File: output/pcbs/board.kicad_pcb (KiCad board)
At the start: 2 copper layers, 122.3 x 101.1 mm, 39 parts

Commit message: wip
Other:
- net class Power added: clearance 0.2, trace_width 0.5, via_dia 0.8, via_drill 0.4
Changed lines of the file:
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@@
 (net 39 "P8")
 (net 40 "P9")
-  (net_class Default "This is the default net class."
+  (net_class Default "This is the default net class"
     (clearance 0.2)
     (trace_width 0.25)
@@
 (add_net "home_thumb")
 (add_net "far_thumb")
-(add_net "RAW")
-(add_net "GND")
 (add_net "RST")
-(add_net "VCC")
 (add_net "P14")
 (add_net "P16")
@@
 (add_net "P9")
   )
+  (net_class Power "This is the power net class"
+    (clearance 0.2)
+    (trace_width 0.5)
+    (via_dia 0.8)
+    (via_drill 0.4)
+    (uvia_dia 0.3)
+    (uvia_drill 0.1)
+    (add_net "RAW")
+(add_net "GND")
+(add_net "VCC")
+  )
       (module PG1350 (layer F.Cu)

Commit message: Add output files
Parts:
- moved REF** 2.00 mm to (122.0, -2.20)
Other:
- outline, holes or cut-outs redrawn
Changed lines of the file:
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@@
       )
       (module TRRS-PJ-320A-dual (layer F.Cu)
-      (at 120 -2.1999999999999993 270)
+      (at 122 -2.1999999999999993 270)
       (fp_text reference REF** (at 0 14.2) (layer Dwgs.User) (effects (font (size 1 1) (thickness 0.15))))
       (fp_text value TRRS-PJ-320A-dual (at 0 -5.6) (layer F.Fab) (effects (font (size 1 1) (thickness 0.15))))
@@
 (gr_arc (start 120 -49.85000000000001) (end 122 -49.85000000000001) (angle -90) (layer Edge.Cuts) (width 0.15))
 (gr_line (start 120 -51.85000000000001) (end 99.9943671 -51.85) (angle 90) (layer Edge.Cuts) (width 0.15))
-(gr_circle (center 27 -28.9) (end 28.9 -28.9) (layer Edge.Cuts) (width 0.15))
-(gr_circle (center 27 0) (end 28.9 0) (layer Edge.Cuts) (width 0.15))
-(gr_circle (center 81 -44.2) (end 82.9 -44.2) (layer Edge.Cuts) (width 0.15))
-(gr_circle (center 72 6.119999999999999) (end 73.9 6.119999999999999) (layer Edge.Cuts) (width 0.15))
-(gr_circle (center 110.3491337 22.311939099999996) (end 112.2491337 22.311939099999996) (layer Edge.Cuts) (width 0.15))
+(gr_circle (center 27 -28.9) (end 29.05 -28.9) (layer Edge.Cuts) (width 0.15))
+(gr_circle (center 27 0) (end 29.05 0) (layer Edge.Cuts) (width 0.15))
+(gr_circle (center 81 -44.2) (end 83.05 -44.2) (layer Edge.Cuts) (width 0.15))
+(gr_circle (center 72 6.119999999999999) (end 74.05 6.119999999999999) (layer Edge.Cuts) (width 0.15))
+(gr_circle (center 110.3491337 22.311939099999996) (end 112.3991337 22.311939099999996) (layer Edge.Cuts) (width 0.15))
 )

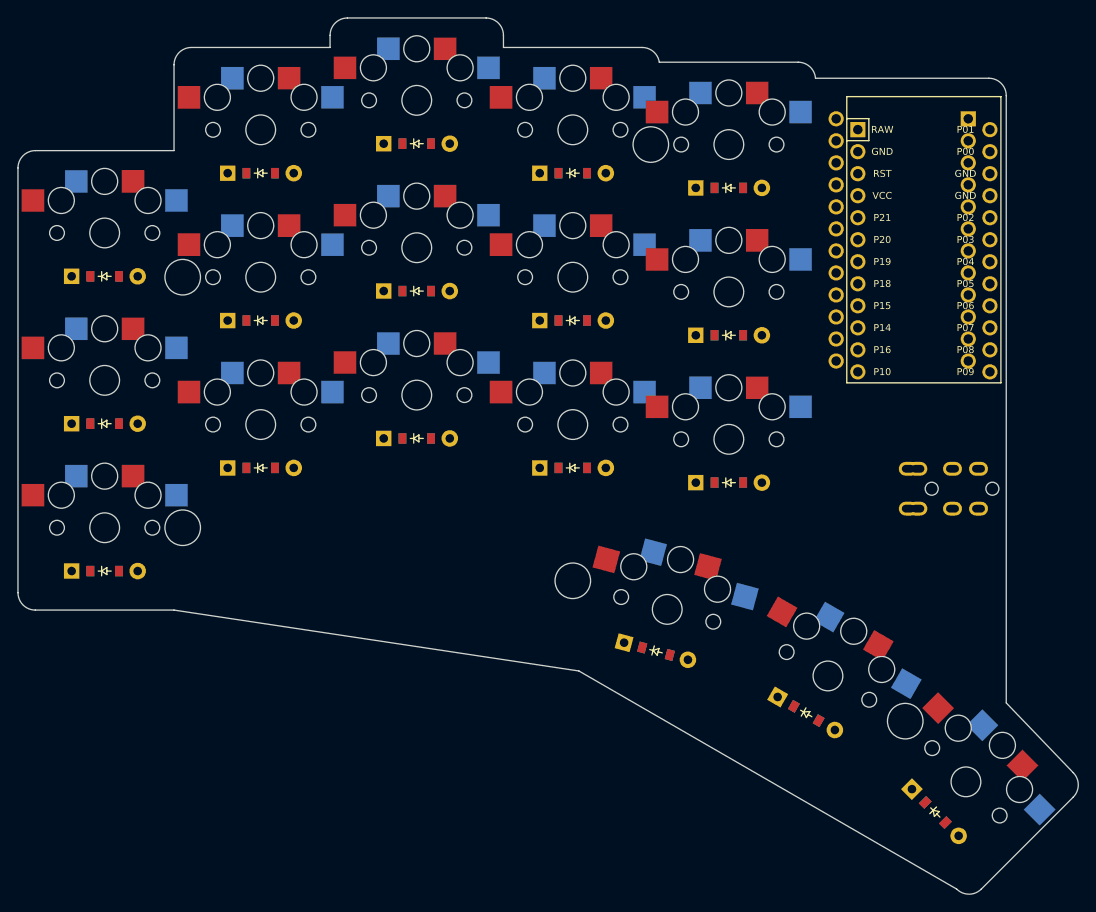
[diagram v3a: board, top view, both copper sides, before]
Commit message: Fix pinout (#3)
* Fix pin compatibility with Corne
* Add battery pins for nice!nano
* Add reset microswitch
* Fix TRRS reversibility
* Add a slider to shut off battery
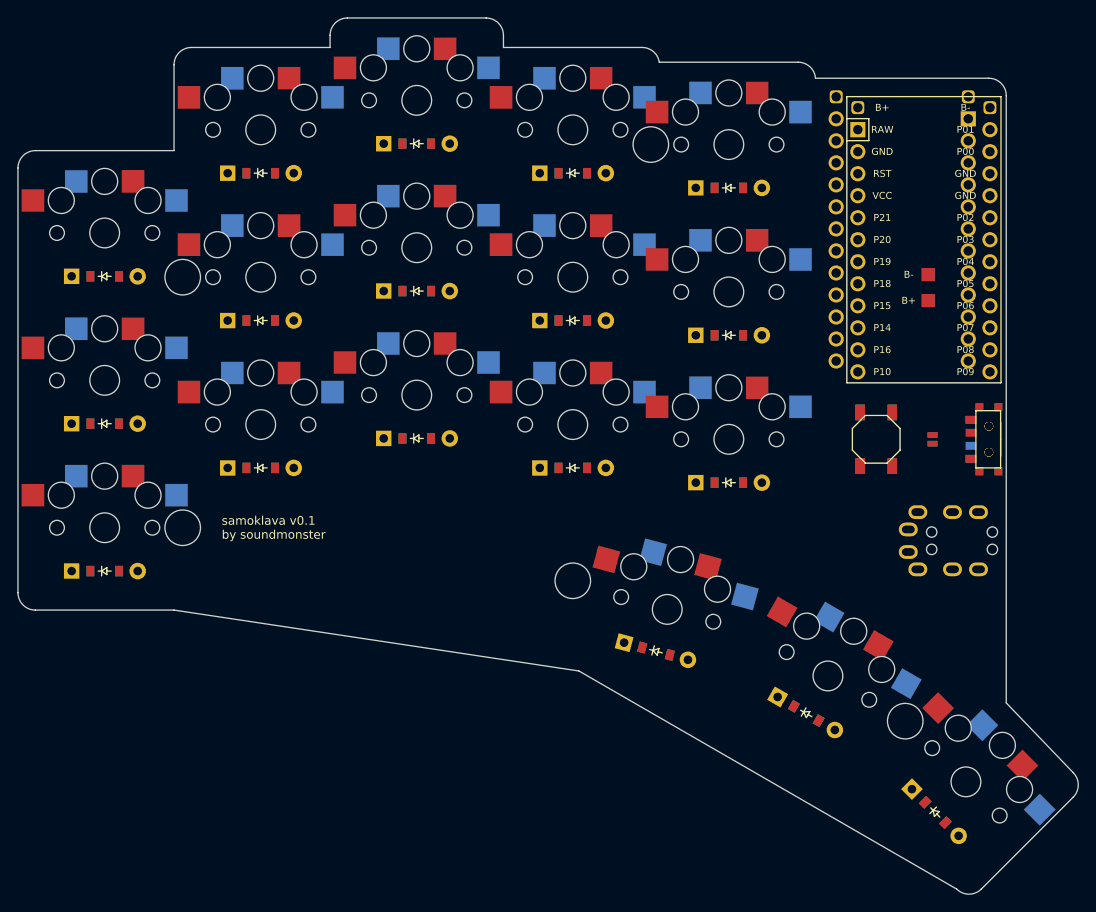
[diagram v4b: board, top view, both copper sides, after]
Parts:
- removed REF**: TRRS-PJ-320A-dual, TRRS-PJ-320A-dual
- added B1, B2: , E73:SW_TACT_ALPS_SKQGABE010, F.Cu at (107.0, -10.2)
- added J1, J2: Jumper, lib:Jumper, F.Cu at (113.5, -10.2)
- added PAD1: , SMDPad, F.Cu at (113.0, -26.2)
- added PAD2: , SMDPad, F.Cu at (113.0, -29.2)
- added T1, T2: , E73:SPDT_C128955, F.Cu at (120.0, -10.2)
- added TRRS1: TRRS-PJ-320A-dual, TRRS-PJ-320A-dual, F.Cu at (122.0, 4.80)
- added TRRS2: TRRS-PJ-320A-dual, TRRS-PJ-320A-dual, F.Cu at (122.0, 2.80)
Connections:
- D1 pad 2: P7 -> P6
- D10 pad 2: P7 -> P6
- D11 pad 2: P6 -> P5
- D12 pad 2: P5 -> P4
- D13 pad 2: P7 -> P6
- D14 pad 2: P6 -> P5
- D15 pad 2: P5 -> P4
- D16 pad 2: P4 -> P7
- D17 pad 2: P4 -> P7
- D18 pad 2: P4 -> P7
- D2 pad 2: P6 -> P5
- D3 pad 2: P5 -> P4
- D4 pad 2: P7 -> P6
- D5 pad 2: P6 -> P5
- D6 pad 2: P5 -> P4
- D7 pad 2: P7 -> P6
- D8 pad 2: P6 -> P5
- D9 pad 2: P5 -> P4
- S1 pad 2: P21 -> P20
- S10 pad 2: P18 -> P15
- S11 pad 2: P18 -> P15
- S12 pad 2: P18 -> P15
- S13 pad 2: P15 -> P14
- S14 pad 2: P15 -> P14
- S15 pad 2: P15 -> P14
- S16 pad 2: P19 -> P18
- S17 pad 2: P18 -> P15
- S18 pad 2: P15 -> P14
- S2 pad 2: P21 -> P20
- S3 pad 2: P21 -> P20
- S4 pad 2: P20 -> P19
- S5 pad 2: P20 -> P19
- S6 pad 2: P20 -> P19
- S7 pad 2: P19 -> P18
- S8 pad 2: P19 -> P18
- S9 pad 2: P19 -> P18
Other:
- board text added: "samoklava v0.1 by soundmonster"
